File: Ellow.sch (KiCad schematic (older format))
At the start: 26 parts, among them J1 USB_C_Receptacle_USB2.0, J2 M_2_AKey_KB, J3 Conn_01x02_Female, J4 Conn_01x04_Female, J5 Conn_01x04_Female, Q1 A03407, Q2 A03407, U1 AP2112K-3.3, U2 E73-2G4M08S1C, U3 LN2054Y42AMR, Y1 32.768kHz

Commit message: routing done, R0
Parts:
- removed J4: Conn_01x04_Female, ellow:PinHeader_1x04_P2.54mm_Vertical_small, symbol Connector:Conn_01x04_Female
- added H2: MountingHole, ellow:MountingHole_M.2_3mm, symbol Mechanical:MountingHole
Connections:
- net GND: now also J2.6; no longer J2.1
- net P0.02: now also D3.2 (A), J2.38
- net P0.03: now also J2.50
- net P0.06: now also J2.27
- net P0.07: now also J2.43; no longer D3.2 (A)
- net P0.08: now also J2.31
- net P0.12: now also J2.39
- net P0.26: now also J2.23
- net P0.28: now also J2.46
- net P1.11: now also J2.66
- net PROG: now also R8.1, U3.5 (PROG)
- net VBAT: no longer J2.5
- net VBUS: now also D2.2 (A), U3.4 (VIN)
- net P0.05: now reaches U2.15 (P0.05/AIN3)
- net P1.09: now reaches U2.17 (P1.09)
- net P0.04: now reaches U2.18 (P0.04/AIN2)
- net P0.04: now also J2.35
- net P1.10: now reaches U2.2 (P1.10)
- net P1.10: now also J2.62
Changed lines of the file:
@@
 Wire Wire Line
 	7200 6100 7100 6100
-Text GLabel 6650 1400 0    50   Input ~ 0
-VBAT
-$Comp
-L power:GND #PWR0104
-U 1 1 5FBE92AA
-P 6450 1200
-F 0 "#PWR0104" H 6450 950 50  0001 C CNN
-F 1 "GND" H 6455 1027 50  0000 C CNN
-F 2 "" H 6450 1200 50  0001 C CNN
-F 3 "" H 6450 1200 50  0001 C CNN
-	1    6450 1200
-	0    1    1    0
-$EndComp
 $Comp
 L ELLOW:M_2_AKey_KB J2
@@
 	1    0    0    -1
 $EndComp
-Wire Wire Line
-	6650 1200 6450 1200
 $Comp
 L Mechanical:MountingHole H1
@@
 Text GLabel 8900 2700 0    50   Input ~ 0
 SWD
-Text GLabel 8900 2100 0    50   Input ~ 0
-DATA+
-Text GLabel 8900 2200 0    50   Input ~ 0
-DATA-
 Text GLabel 3250 4400 1    50   Input ~ 0
 P0.26
@@
 	1    0    0    -1
 $EndComp
-$Comp
-L Connector:Conn_01x04_Female J4
-U 1 1 5FDB58A8
-P 9100 2000
-F 0 "J4" H 9128 1976 50  0000 L CNN
-F 1 "Conn_01x04_Female" H 9128 1885 50  0000 L CNN
-F 2 "ellow:PinHeader_1x04_P2.54mm_Vertical_small" H 9100 2000 50  0001 C CNN
-F 3 "~" H 9100 2000 50  0001 C CNN
-	1    9100 2000
-	1    0    0    -1
-$EndComp
-Text GLabel 8900 1900 0    50   Input ~ 0
-GND
-Text GLabel 8900 2000 0    50   Input ~ 0
-VBUS
 Text GLabel 6650 4250 0    50   Input ~ 0
 P1.02
@@
 P0.07
 Text GLabel 4250 4200 0    50   Input ~ 0
-P0.07
+P0.02
 Text GLabel 6650 3650 0    50   Input ~ 0
 P0.20
@@
 Text GLabel 7150 1700 2    50   Input ~ 0
 GND
+Text GLabel 2750 4350 1    50   Input ~ 0
+P1.09
+Text GLabel 2650 4400 1    50   Input ~ 0
+P0.04
+Text GLabel 2950 4350 1    50   Input ~ 0
+P0.05
+$Comp
+L Mechanical:MountingHole H2
+U 1 1 5FBD39D8
+P 9950 900
+F 0 "H2" H 10050 946 50  0000 L CNN
+F 1 "MountingHole" H 10050 855 50  0000 L CNN
+F 2 "ellow:MountingHole_M.2_3mm" H 9950 900 50  0001 C CNN
+F 3 "~" H 9950 900 50  0001 C CNN
+	1    9950 900
+	1    0    0    -1
+$EndComp
+Text GLabel 6650 3050 0    50   Input ~ 0
+P0.07
+Text GLabel 6650 2850 0    50   Input ~ 0
+P0.12
+Text GLabel 6650 2650 0    50   Input ~ 0
+P0.04
+Text GLabel 6650 2450 0    50   Input ~ 0
+P0.08
+Text GLabel 6650 2250 0    50   Input ~ 0
+P0.06
+Text GLabel 6650 2050 0    50   Input ~ 0
+P0.26
+Text GLabel 3600 6200 2    50   Input ~ 0
+P1.10
+Text GLabel 7150 4000 2    50   Input ~ 0
+P1.10
+Text GLabel 7150 4200 2    50   Input ~ 0
+P1.11
+Text GLabel 7150 3400 2    50   Input ~ 0
+P0.03
+Text GLabel 7150 3200 2    50   Input ~ 0
+P0.28
+Text GLabel 7150 2800 2    50   Input ~ 0
+P0.02
+Text GLabel 4750 1550 2    50   Input ~ 0
+PROG
+Wire Wire Line
+	4650 1550 4750 1550
+Connection ~ 4650 1550
+Text GLabel 4650 1350 2    50   Input ~ 0
+VBUS
+Wire Wire Line
+	4650 1350 4550 1350
+Connection ~ 4550 1350
+Text GLabel 7150 1450 2    50   Input ~ 0
+GND
 $EndSCHEMATC

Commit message: EOD
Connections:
- net GND: no longer J2.17
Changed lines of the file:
@@
 Text GLabel 7150 1250 2    50   Input ~ 0
 EXT_VCC
-Text GLabel 6650 1750 0    50   Input ~ 0
-GND
 Text GLabel 6650 4650 0    50   Input ~ 0
 P1.06

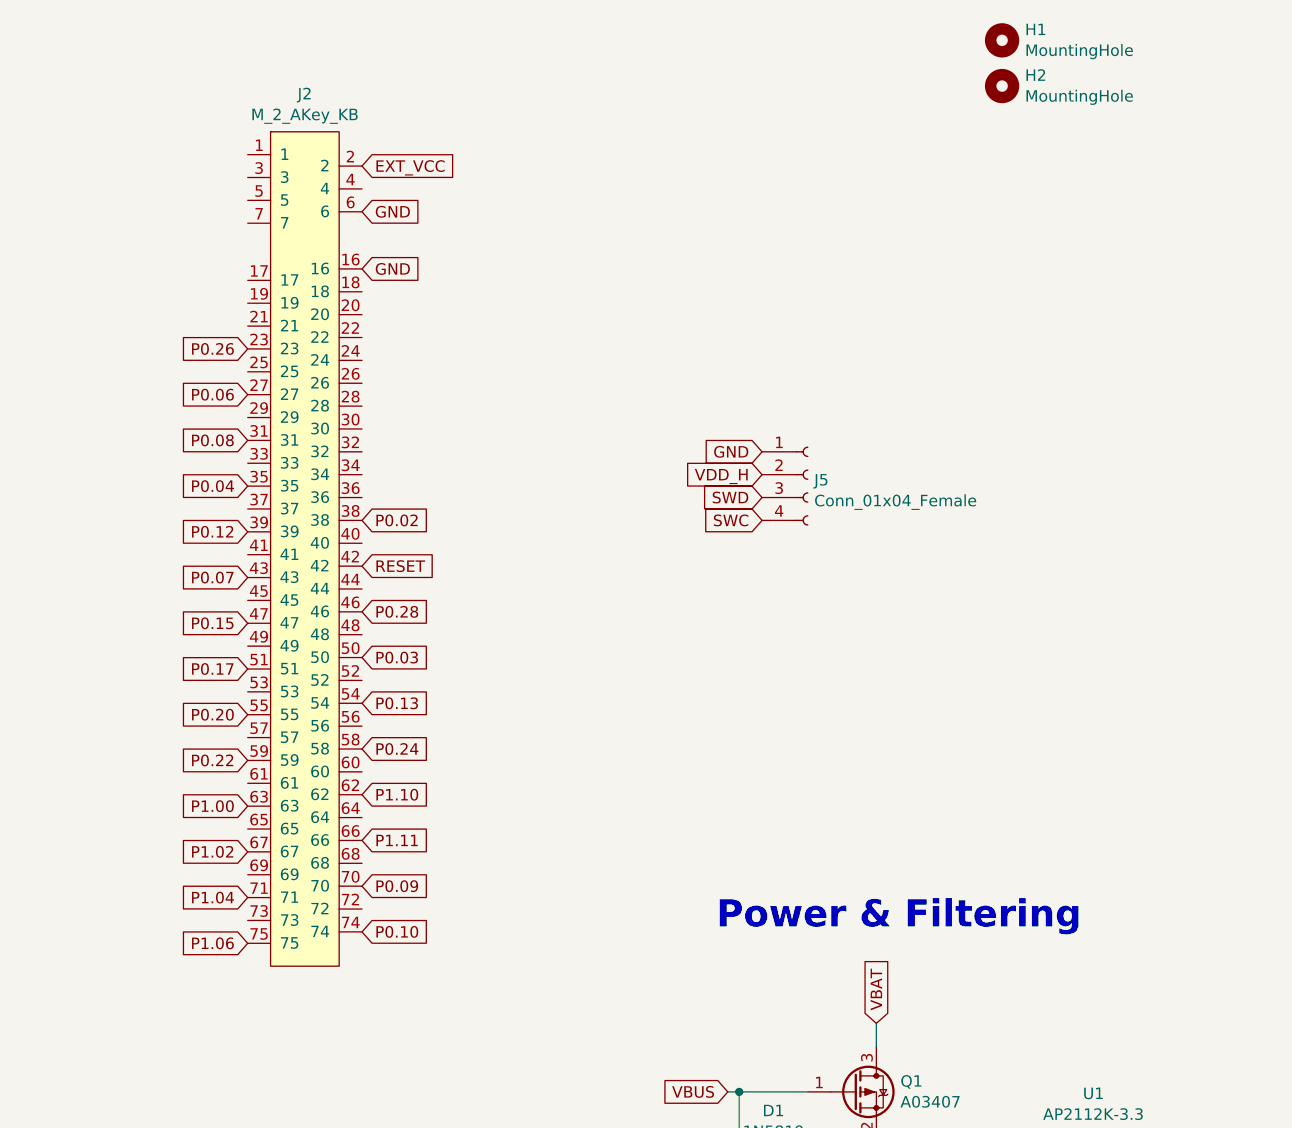
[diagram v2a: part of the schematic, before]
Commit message: first autoroute attempt
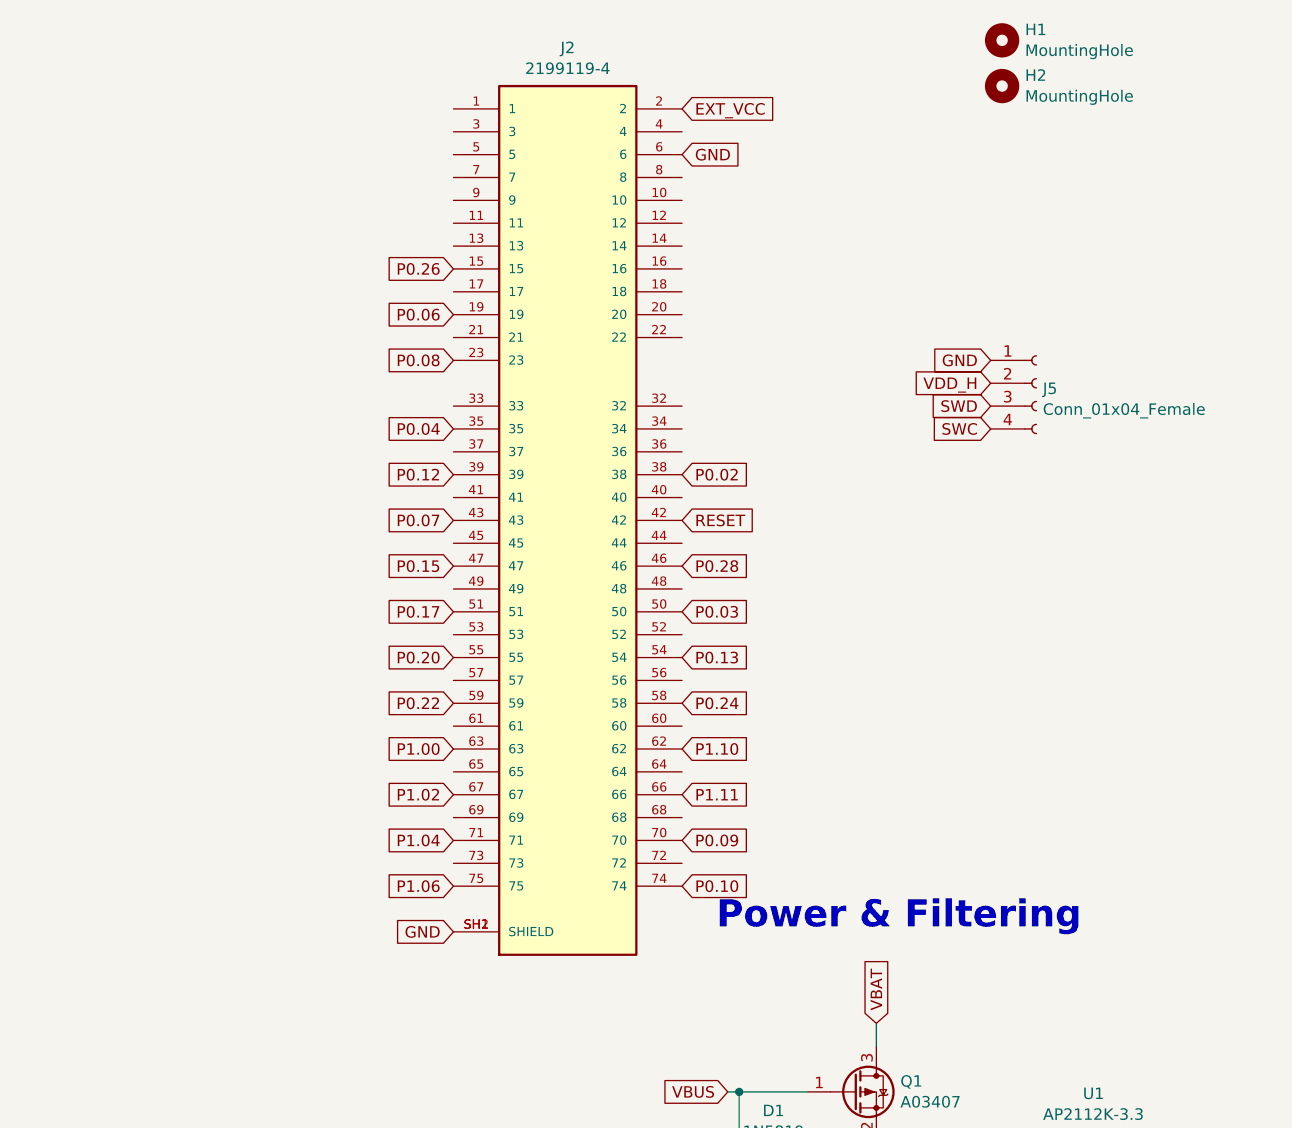
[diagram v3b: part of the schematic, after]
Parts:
- removed J2: M_2_AKey_KB, ellow:M_2_EdgeConnector_A_Key, symbol ELLOW:M_2_AKey_KB
- added J2: 2199119-4, ellow:M_2_EdgeConnector_E_Key, symbol ELLOW:2199119-4
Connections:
- net EXT_VCC: now also J2.2
- net GND: now also J2.6, J2.SH1 (SHIELD), J2.SH2 (SHIELD)
- net P0.02: now also J2.38
- net P0.03: now also J2.50
- net P0.04: now also J2.35
- net P0.06: now also J2.19
- net P0.07: now also J2.43
- net P0.08: now also J2.23
- net P0.09: now also J2.70
- net P0.10: now also J2.74
- net P0.12: now also J2.39
- net P0.13: now also J2.54
- net P0.15: now also J2.47
- net P0.17: now also J2.51
- net P0.20: now also J2.55
- net P0.22: now also J2.59
- net P0.24: now also J2.58
- net P0.26: now also J2.15
- net P0.28: now also J2.46
- net P1.00: now also J2.63
- net P1.02: now also J2.67
- net P1.04: now also J2.71
- net P1.06: now also J2.75
- net P1.10: now also J2.62
- net P1.11: now also J2.66
- net RESET: now also J2.42
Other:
- moved on the sheet: J5
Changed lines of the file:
@@
 Wire Wire Line
 	9950 5650 10050 5650
-Text GLabel 10750 5550 2    50   Input ~ 0
-VDD_H
 Wire Wire Line
 	10650 5550 10750 5550
@@
 Wire Wire Line
 	7200 6100 7100 6100
-$Comp
-L ELLOW:M_2_AKey_KB J2
-U 1 1 5FC057BA
-P 6850 1000
-F 0 "J2" H 6900 1065 50  0000 C CNN
-F 1 "M_2_AKey_KB" H 6900 974 50  0000 C CNN
-F 2 "ellow:M_2_EdgeConnector_A_Key" H 6850 1000 50  0001 C CNN
-F 3 "" H 6850 1000 50  0001 C CNN
-	1    6850 1000
-	1    0    0    -1
-$EndComp
 $Comp
 L Mechanical:MountingHole H1
@@
 Text GLabel 3600 5700 2    50   Input ~ 0
 P0.02
-Text GLabel 7150 3000 2    50   Input ~ 0
+Text GLabel 8550 2800 2    50   Input ~ 0
 RESET
-Text GLabel 7150 1250 2    50   Input ~ 0
+Text GLabel 8550 1000 2    50   Input ~ 0
 EXT_VCC
-Text GLabel 6650 4650 0    50   Input ~ 0
+Text GLabel 7550 4400 0    50   Input ~ 0
 P1.06
-Text GLabel 7150 4600 2    50   Input ~ 0
+Text GLabel 8550 4400 2    50   Input ~ 0
 P0.10
-Text GLabel 7150 3800 2    50   Input ~ 0
+Text GLabel 8550 3600 2    50   Input ~ 0
 P0.24
-Text GLabel 6650 3450 0    50   Input ~ 0
+Text GLabel 7550 3200 0    50   Input ~ 0
 P0.17
-Text GLabel 8900 2500 0    50   Input ~ 0
+Text GLabel 9900 2100 0    50   Input ~ 0
 GND
-Text GLabel 8900 2600 0    50   Input ~ 0
+Text GLabel 9900 2200 0    50   Input ~ 0
 VDD_H
-Text GLabel 8900 2800 0    50   Input ~ 0
+Text GLabel 9900 2400 0    50   Input ~ 0
 SWC
-Text GLabel 8900 2700 0    50   Input ~ 0
+Text GLabel 9900 2300 0    50   Input ~ 0
 SWD
 Text GLabel 3250 4400 1    50   Input ~ 0
@@
 L Connector:Conn_01x04_Female J5
 U 1 1 5FDB4AEC
-P 9100 2600
-F 0 "J5" H 9128 2576 50  0000 L CNN
-F 1 "Conn_01x04_Female" H 9128 2485 50  0000 L CNN
-F 2 "ellow:PinHeader_1x04_P2.54mm_Vertical_small" H 9100 2600 50  0001 C CNN
-F 3 "~" H 9100 2600 50  0001 C CNN
-	1    9100 2600
-	1    0    0    -1
-$EndComp
-Text GLabel 6650 4250 0    50   Input ~ 0
+P 10100 2200
+F 0 "J5" H 10128 2176 50  0000 L CNN
+F 1 "Conn_01x04_Female" H 10128 2085 50  0000 L CNN
+F 2 "ellow:PinHeader_1x04_P2.54mm_Vertical_small" H 10100 2200 50  0001 C CNN
+F 3 "~" H 10100 2200 50  0001 C CNN
+	1    10100 2200
+	1    0    0    -1
+$EndComp
+Text GLabel 7550 4000 0    50   Input ~ 0
 P1.02
-Text GLabel 6650 4050 0    50   Input ~ 0
+Text GLabel 7550 3800 0    50   Input ~ 0
 P1.00
-Text GLabel 6650 3850 0    50   Input ~ 0
+Text GLabel 7550 3600 0    50   Input ~ 0
 P0.22
-Text GLabel 7150 3600 2    50   Input ~ 0
+Text GLabel 8550 3400 2    50   Input ~ 0
 P0.13
-Text GLabel 6650 3250 0    50   Input ~ 0
+Text GLabel 7550 3000 0    50   Input ~ 0
 P0.15
 $Comp
@@
 Text GLabel 4250 4200 0    50   Input ~ 0
 P0.02
-Text GLabel 6650 3650 0    50   Input ~ 0
+Text GLabel 7550 3400 0    50   Input ~ 0
 P0.20
-Text GLabel 7150 4400 2    50   Input ~ 0
+Text GLabel 8550 4200 2    50   Input ~ 0
 P0.09
-Text GLabel 6650 4450 0    50   Input ~ 0
+Text GLabel 7550 4200 0    50   Input ~ 0
 P1.04
-Text GLabel 7150 1700 2    50   Input ~ 0
+Text GLabel 8550 1200 2    50   Input ~ 0
 GND
 Text GLabel 2750 4350 1    50   Input ~ 0
@@
 	1    0    0    -1
 $EndComp
-Text GLabel 6650 3050 0    50   Input ~ 0
+Text GLabel 7550 2800 0    50   Input ~ 0
 P0.07
-Text GLabel 6650 2850 0    50   Input ~ 0
+Text GLabel 7550 2600 0    50   Input ~ 0
 P0.12
-Text GLabel 6650 2650 0    50   Input ~ 0
+Text GLabel 7550 2400 0    50   Input ~ 0
 P0.04
-Text GLabel 6650 2450 0    50   Input ~ 0
+Text GLabel 7550 2100 0    50   Input ~ 0
 P0.08
-Text GLabel 6650 2250 0    50   Input ~ 0
+Text GLabel 7550 1900 0    50   Input ~ 0
 P0.06
-Text GLabel 6650 2050 0    50   Input ~ 0
+Text GLabel 7550 1700 0    50   Input ~ 0
 P0.26
 Text GLabel 3600 6200 2    50   Input ~ 0
 P1.10
-Text GLabel 7150 4000 2    50   Input ~ 0
+Text GLabel 8550 3800 2    50   Input ~ 0
 P1.10
-Text GLabel 7150 4200 2    50   Input ~ 0
+Text GLabel 8550 4000 2    50   Input ~ 0
 P1.11
-Text GLabel 7150 3400 2    50   Input ~ 0
+Text GLabel 8550 3200 2    50   Input ~ 0
 P0.03
-Text GLabel 7150 3200 2    50   Input ~ 0
+Text GLabel 8550 3000 2    50   Input ~ 0
 P0.28
-Text GLabel 7150 2800 2    50   Input ~ 0
+Text GLabel 8550 2600 2    50   Input ~ 0
 P0.02
 Text GLabel 4750 1550 2    50   Input ~ 0
@@
 	4650 1350 4550 1350
 Connection ~ 4550 1350
-Text GLabel 7150 1450 2    50   Input ~ 0
+Text GLabel 10750 5550 2    50   Input ~ 0
+VDD_H
+$Comp
+L ELLOW:2199119-4 J2
+U 1 1 5FC6B873
+P 8050 2800
+F 0 "J2" H 8050 4867 50  0000 C CNN
+F 1 "2199119-4" H 8050 4776 50  0000 C CNN
+F 2 "ellow:M_2_EdgeConnector_E_Key" H 8050 2800 50  0001 L BNN
+F 3 "" H 8050 2800 50  0001 L BNN
+F 4 "2199119-4" H 8050 2800 50  0001 L BNN "Comment"
+	1    8050 2800
+	1    0    0    -1
+$EndComp
+Text GLabel 7550 4600 0    50   Input ~ 0
 GND
 $EndSCHEMATC

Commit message: routed and ready for QA check
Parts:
- added SW1: SW_Push, Button_Switch_SMD:SW_SPST_B3U-1000P, symbol Switch:SW_Push
- J2: symbol ELLOW:2199119-4 -> Ellow-rescue:2199119-4-ELLOW
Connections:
- net EXT_VCC: now also J2.74; no longer J2.2
- net GND: now also J2.75, SW1.2; no longer J2.6
- net P0.02: now also J2.37; no longer J2.38
- net P0.03: no longer J2.50
- net P0.04: now also J2.56; no longer J2.35
- net P0.06: now also J2.64; no longer J2.19
- net P0.07: now also J2.48; no longer J2.43
- net P0.08: now also J2.60; no longer J2.23
- net P0.09: now also J2.5; no longer J2.70
- net P0.10: now also J2.1; no longer J2.74
- net P0.12: now also J2.52; no longer J2.39
- net P0.13: now also J2.21; no longer J2.54
- net P0.15: now also J2.44; no longer J2.47
- net P0.17: now also J2.40; no longer J2.51
- net P0.20: now also J2.36; no longer J2.55
- net P0.22: now also J2.32; no longer J2.59
- net P0.24: now also J2.17; no longer J2.58
- net P0.26: now also J2.68; no longer J2.15
- net P0.28: now also J2.33; no longer J2.46
- net P1.00: now also J2.22; no longer J2.63
- net P1.02: now also J2.18; no longer J2.67
- net P1.04: now also J2.14; no longer J2.71
- net P1.06: now also J2.10; no longer J2.75
- net P1.10: now also J2.13; no longer J2.62
- net P1.11: now also J2.9; no longer J2.66
- net RESET: now also J2.57, SW1.1; no longer J2.42
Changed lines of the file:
@@
 Text GLabel 3600 5700 2    50   Input ~ 0
 P0.02
-Text GLabel 8550 2800 2    50   Input ~ 0
+Text GLabel 7550 3500 0    50   Input ~ 0
 RESET
-Text GLabel 8550 1000 2    50   Input ~ 0
+Text GLabel 8550 4400 2    50   Input ~ 0
 EXT_VCC
-Text GLabel 7550 4400 0    50   Input ~ 0
+Text GLabel 8550 1400 2    50   Input ~ 0
 P1.06
-Text GLabel 8550 4400 2    50   Input ~ 0
+Text GLabel 7550 1000 0    50   Input ~ 0
 P0.10
-Text GLabel 8550 3600 2    50   Input ~ 0
+Text GLabel 7550 1800 0    50   Input ~ 0
 P0.24
-Text GLabel 7550 3200 0    50   Input ~ 0
+Text GLabel 8550 2700 2    50   Input ~ 0
 P0.17
 Text GLabel 9900 2100 0    50   Input ~ 0
@@
 	1    0    0    -1
 $EndComp
-Text GLabel 7550 4000 0    50   Input ~ 0
+Text GLabel 8550 1800 2    50   Input ~ 0
 P1.02
-Text GLabel 7550 3800 0    50   Input ~ 0
+Text GLabel 8550 2000 2    50   Input ~ 0
 P1.00
-Text GLabel 7550 3600 0    50   Input ~ 0
+Text GLabel 8550 2300 2    50   Input ~ 0
 P0.22
-Text GLabel 8550 3400 2    50   Input ~ 0
+Text GLabel 7550 2000 0    50   Input ~ 0
 P0.13
-Text GLabel 7550 3000 0    50   Input ~ 0
+Text GLabel 8550 2900 2    50   Input ~ 0
 P0.15
 $Comp
@@
 Text GLabel 4250 4200 0    50   Input ~ 0
 P0.02
-Text GLabel 7550 3400 0    50   Input ~ 0
+Text GLabel 8550 2500 2    50   Input ~ 0
 P0.20
-Text GLabel 8550 4200 2    50   Input ~ 0
+Text GLabel 7550 1200 0    50   Input ~ 0
 P0.09
-Text GLabel 7550 4200 0    50   Input ~ 0
+Text GLabel 8550 1600 2    50   Input ~ 0
 P1.04
-Text GLabel 8550 1200 2    50   Input ~ 0
+Text GLabel 7550 4400 0    50   Input ~ 0
 GND
 Text GLabel 2750 4350 1    50   Input ~ 0
@@
 	1    0    0    -1
 $EndComp
-Text GLabel 7550 2800 0    50   Input ~ 0
+Text GLabel 8550 3100 2    50   Input ~ 0
 P0.07
-Text GLabel 7550 2600 0    50   Input ~ 0
+Text GLabel 8550 3300 2    50   Input ~ 0
 P0.12
-Text GLabel 7550 2400 0    50   Input ~ 0
+Text GLabel 8550 3500 2    50   Input ~ 0
 P0.04
-Text GLabel 7550 2100 0    50   Input ~ 0
+Text GLabel 8550 3700 2    50   Input ~ 0
 P0.08
-Text GLabel 7550 1900 0    50   Input ~ 0
+Text GLabel 8550 3900 2    50   Input ~ 0
 P0.06
-Text GLabel 7550 1700 0    50   Input ~ 0
+Text GLabel 8550 4100 2    50   Input ~ 0
 P0.26
 Text GLabel 3600 6200 2    50   Input ~ 0
 P1.10
-Text GLabel 8550 3800 2    50   Input ~ 0
+Text GLabel 7550 1600 0    50   Input ~ 0
 P1.10
-Text GLabel 8550 4000 2    50   Input ~ 0
-P1.11
-Text GLabel 8550 3200 2    50   Input ~ 0
-P0.03
-Text GLabel 8550 3000 2    50   Input ~ 0
+Text GLabel 7550 2300 0    50   Input ~ 0
 P0.28
-Text GLabel 8550 2600 2    50   Input ~ 0
+Text GLabel 7550 2500 0    50   Input ~ 0
 P0.02
 Text GLabel 4750 1550 2    50   Input ~ 0
@@
 VDD_H
 $Comp
-L ELLOW:2199119-4 J2
+L Ellow-rescue:2199119-4-ELLOW J2
 U 1 1 5FC6B873
 P 8050 2800
@@
 Text GLabel 7550 4600 0    50   Input ~ 0
 GND
+Text GLabel 7550 1400 0    50   Input ~ 0
+P1.11
+$Comp
+L Switch:SW_Push SW1
+U 1 1 5FCCB900
+P 6050 3300
+F 0 "SW1" H 6050 3585 50  0000 C CNN
+F 1 "SW_Push" H 6050 3494 50  0000 C CNN
+F 2 "Button_Switch_SMD:SW_SPST_B3U-1000P" H 6050 3500 50  0001 C CNN
+F 3 "~" H 6050 3500 50  0001 C CNN
+	1    6050 3300
+	1    0    0    -1
+$EndComp
+Text GLabel 5850 3300 0    50   Input ~ 0
+RESET
+$Comp
+L power:GND #PWR0104
+U 1 1 5FCCE3C8
+P 6250 3300
+F 0 "#PWR0104" H 6250 3050 50  0001 C CNN
+F 1 "GND" H 6255 3127 50  0000 C CNN
+F 2 "" H 6250 3300 50  0001 C CNN
+F 3 "" H 6250 3300 50  0001 C CNN
+	1    6250 3300
+	1    0    0    -1
+$EndComp
 $EndSCHEMATC
